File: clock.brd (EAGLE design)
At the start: 100 x 80 mm, 50 parts, among them J3 POWER_JACKSLT, U2 LM75A_SO8, U3 ESP8266_13

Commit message: Worked on the silk
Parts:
- moved TP3 0.76 mm to (18.7, 27.6)
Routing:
- net N$2: track 14.4 -> 13.7 mm
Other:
- board text added: "0318"
- board text added: "1: ADC"
- board text added: "2: LED Data (3V)"
- board text added: "3: LED Data (5V)"
- board text added: "4: LM75A OS"
- board text added: "5: IO2"
- board text added: "6: IO3"
- board text added: "DATA"
- board text added: "IO12"
- board text added: "IO13"
- board text added: "IO14"
- board text added: "IO15"
- board text added: "IO3"
- board text added: "IO4"
- board text added: "IO5"
- board text added: "Testpoints:"
- board text removed: "0218"
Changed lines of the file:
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@@
 <rectangle x1="2.2" y1="44.1" x2="5.8" y2="45.3" layer="51"/>
 <text x="9" y="78" size="1.016" layer="21" font="vector" ratio="12" align="center-left">Rev A</text>
-<text x="9" y="76.5" size="1.016" layer="21" font="vector" ratio="12" align="center-left">0218</text>
+<text x="9" y="76.5" size="1.016" layer="21" font="vector" ratio="12" align="center-left">0318</text>
 <text x="24.7" y="25" size="1.016" layer="21" font="vector" ratio="12" align="center">G</text>
 <dimension x1="3.5" y1="3.5" x2="96.5" y2="3.5" x3="50" y3="-2.6" textsize="1.016" textratio="12" layer="51" dtype="horizontal"/>
@@
 <wire x1="90.99" y1="19.5" x2="90.59" y2="19.9" width="0.127" layer="21"/>
 <wire x1="90.99" y1="18.3" x2="90.59" y2="18.7" width="0.127" layer="21"/>
+<wire x1="22" y1="44" x2="27.6" y2="44" width="0.127" layer="21"/>
+<wire x1="22" y1="36" x2="27.6" y2="36" width="0.127" layer="21"/>
+<wire x1="22" y1="44" x2="22" y2="36" width="0.127" layer="21"/>
+<text x="21" y="40" size="1.016" layer="21" font="vector" ratio="12" rot="R180" align="center-left">DATA</text>
+<wire x1="22" y1="57" x2="27.6" y2="57" width="0.127" layer="21"/>
+<wire x1="22" y1="51" x2="27.6" y2="51" width="0.127" layer="21"/>
+<wire x1="22" y1="57" x2="22" y2="51" width="0.127" layer="21"/>
+<text x="25" y="69.5" size="1.016" layer="22" font="vector" ratio="12" rot="MR0" align="center-left">Testpoints:</text>
+<text x="25" y="66.5" size="1.016" layer="22" font="vector" ratio="12" rot="MR0" align="center-left">1: ADC</text>
+<text x="25" y="64.5" size="1.016" layer="22" font="vector" ratio="12" rot="MR0" align="center-left">2: LED Data (3V)</text>
+<text x="25" y="62.5" size="1.016" layer="22" font="vector" ratio="12" rot="MR0" align="center-left">3: LED Data (5V)</text>
+<text x="25" y="60.5" size="1.016" layer="22" font="vector" ratio="12" rot="MR0" align="center-left">4: LM75A OS</text>
+<text x="25" y="58.5" size="1.016" layer="22" font="vector" ratio="12" rot="MR0" align="center-left">5: IO2</text>
+<text x="25" y="56.5" size="1.016" layer="22" font="vector" ratio="12" rot="MR0" align="center-left">6: IO3</text>
+<wire x1="26" y1="71" x2="26" y2="68" width="0.127" layer="22"/>
+<wire x1="26" y1="68" x2="26" y2="55" width="0.127" layer="22"/>
+<wire x1="26" y1="55" x2="11" y2="55" width="0.127" layer="22"/>
+<wire x1="11" y1="55" x2="11" y2="68" width="0.127" layer="22"/>
+<wire x1="11" y1="68" x2="11" y2="71" width="0.127" layer="22"/>
+<wire x1="26" y1="71" x2="11" y2="71" width="0.127" layer="22"/>
+<wire x1="26" y1="68" x2="11" y2="68" width="0.127" layer="22"/>
+<text x="7.1" y="17.54" size="0.6096" layer="22" font="vector" ratio="12" rot="MR270" align="top-center">IO12</text>
+<text x="7.1" y="15" size="0.6096" layer="22" font="vector" ratio="12" rot="MR270" align="top-center">IO15</text>
+<text x="7.1" y="12.46" size="0.6096" layer="22" font="vector" ratio="12" rot="MR270" align="top-center">IO3</text>
+<text x="7.1" y="9.92" size="0.6096" layer="21" font="vector" ratio="12" rot="R90" align="top-center">SDA</text>
+<text x="7.1" y="9.92" size="0.6096" layer="22" font="vector" ratio="12" rot="MR270" align="top-center">IO4</text>
+<text x="1.1" y="9.92" size="0.6096" layer="22" font="vector" ratio="12" rot="MR270" align="bottom-center">IO5</text>
+<text x="1" y="15" size="0.6096" layer="22" font="vector" ratio="12" rot="MR270" align="bottom-center">IO13</text>
+<text x="1" y="17.54" size="0.6096" layer="22" font="vector" ratio="12" rot="MR270" align="bottom-center">IO14</text>
 </plain>
 <attributes>
@@
 </element>
 <element name="J2" library="Sebastian" package="IEC_C8_RIGHT" value="" x="91" y="60" rot="R270"/>
-<element name="U3" library="Sebastian" package="ESP13" value="ESP8266_13" x="20.5" y="4" rot="R180"/>
+<element name="U3" library="Sebastian" package="ESP13" value="ESP8266_13" x="20.5" y="4" smashed="yes" rot="R180">
+<attribute name="NAME" x="29.5" y="15" size="1.016" layer="25" font="vector" ratio="12" rot="R180" align="center-left"/>
+</element>
 <element name="JP1" library="Sebastian" package="1X3_MOLEX_53254" value="" x="28" y="40" rot="R90"/>
 <element name="J5" library="Sebastian" package="1X2_MOLEX_53254" value="" x="28" y="54" rot="R90"/>
@@
 <attribute name="VALUE" x="18.065" y="24.338" size="0.0254" layer="27"/>
 </element>
-<element name="TP3" library="testpad" package="TP15R" value="TPTP15R" x="18.7" y="28.4" smashed="yes">
-<attribute name="NAME" x="18.7" y="26.8" size="1.016" layer="25" font="vector" ratio="12" align="center"/>
-<attribute name="TP_SIGNAL_NAME" value="" x="18.7" y="25.86" size="1" layer="37"/>
-<attribute name="VALUE" x="18.065" y="27.638" size="0.0254" layer="27"/>
+<element name="TP3" library="testpad" package="TP15R" value="TPTP15R" x="18.7" y="27.64" smashed="yes">
+<attribute name="NAME" x="18.7" y="29.24" size="1.016" layer="25" font="vector" ratio="12" align="center"/>
+<attribute name="TP_SIGNAL_NAME" value="" x="18.7" y="25.1" size="1" layer="37"/>
+<attribute name="VALUE" x="18.065" y="26.878" size="0.0254" layer="27"/>
 </element>
 <element name="TP4" library="testpad" package="TP15R" value="TPTP15R" x="4.5" y="52" smashed="yes">
@@
 <contactref element="TP3" pad="TP"/>
 <wire x1="14.325" y1="21.98740625" x2="16.08740625" y2="21.98740625" width="0.254" layer="1"/>
-<wire x1="16.08740625" y1="21.98740625" x2="17.3" y2="23.2" width="0.254" layer="1"/>
-<wire x1="17.3" y1="23.2" x2="17.3" y2="27" width="0.254" layer="1"/>
-<wire x1="17.3" y1="27" x2="18.7" y2="28.4" width="0.254" layer="1"/>
+<wire x1="17.3" y1="23.2" x2="16.08740625" y2="21.98740625" width="0.254" layer="1"/>
+<wire x1="18.7" y1="27.64" x2="17.3" y2="26.24" width="0.254" layer="1"/>
+<wire x1="17.3" y1="26.24" x2="17.3" y2="23.2" width="0.254" layer="1"/>
 </signal>
 <signal name="L">

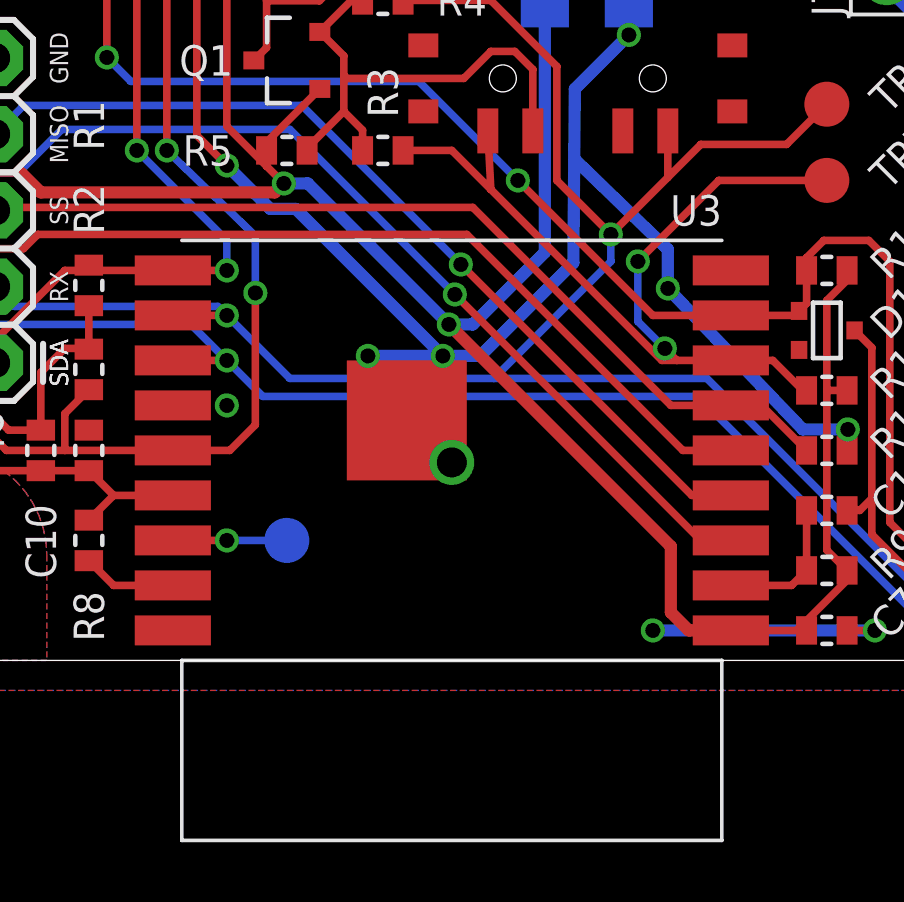
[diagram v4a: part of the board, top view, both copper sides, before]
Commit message: Switched to the new footprint for the ESP8266
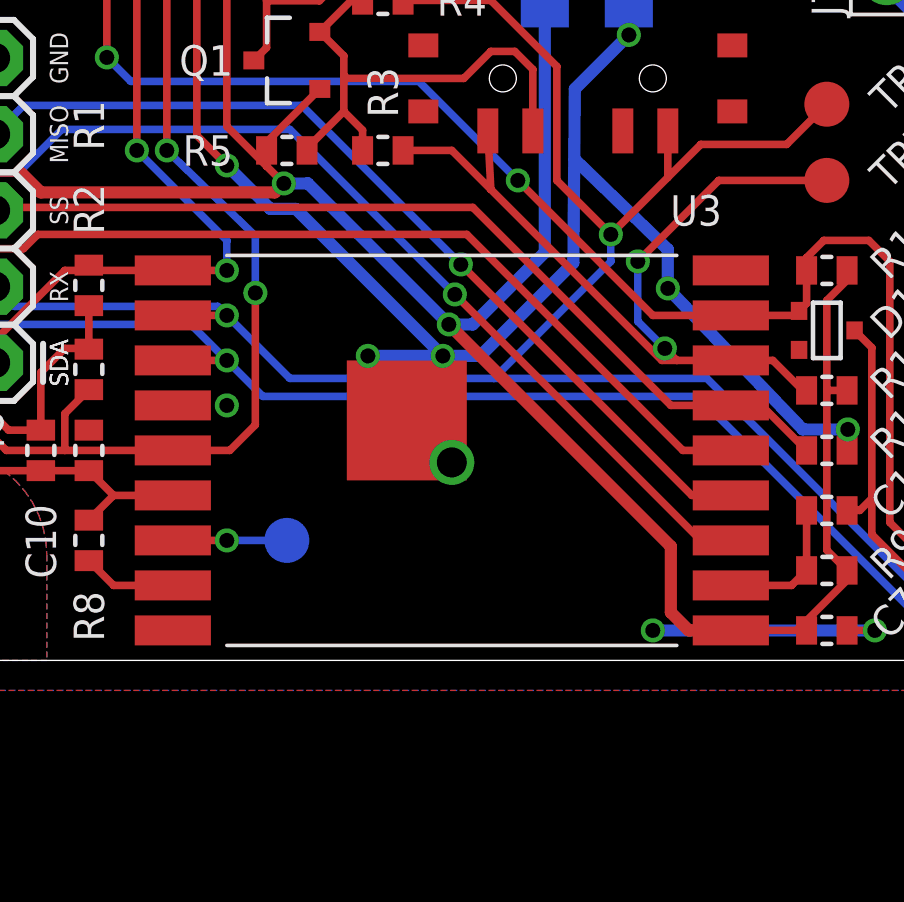
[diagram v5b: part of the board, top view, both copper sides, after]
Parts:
- U3: device Sebastian:ESP13 -> Modules:ESP13
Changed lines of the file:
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@@
 <layers>
 <layer number="1" name="Top" color="4" fill="1" visible="yes" active="yes"/>
+<layer number="2" name="Route2" color="1" fill="3" visible="no" active="no"/>
+<layer number="3" name="Route3" color="4" fill="3" visible="no" active="no"/>
+<layer number="4" name="Route4" color="1" fill="4" visible="no" active="no"/>
+<layer number="5" name="Route5" color="4" fill="4" visible="no" active="no"/>
+<layer number="6" name="Route6" color="1" fill="8" visible="no" active="no"/>
+<layer number="7" name="Route7" color="4" fill="8" visible="no" active="no"/>
+<layer number="8" name="Route8" color="1" fill="2" visible="no" active="no"/>
+<layer number="9" name="Route9" color="4" fill="2" visible="no" active="no"/>
+<layer number="10" name="Route10" color="1" fill="7" visible="no" active="no"/>
+<layer number="11" name="Route11" color="4" fill="7" visible="no" active="no"/>
+<layer number="12" name="Route12" color="1" fill="5" visible="no" active="no"/>
+<layer number="13" name="Route13" color="4" fill="5" visible="no" active="no"/>
+<layer number="14" name="Route14" color="1" fill="6" visible="no" active="no"/>
+<layer number="15" name="Route15" color="4" fill="6" visible="no" active="no"/>
 <layer number="16" name="Bottom" color="1" fill="1" visible="yes" active="yes"/>
 <layer number="17" name="Pads" color="2" fill="1" visible="yes" active="yes"/>
@@
 </element>
 <element name="J2" library="Sebastian" package="IEC_C8_RIGHT" value="" x="91" y="60" rot="R270"/>
-<element name="U3" library="Sebastian" package="ESP13" value="ESP8266_13" x="20.5" y="4" smashed="yes" rot="R180">
-<attribute name="NAME" x="29.5" y="15" size="1.016" layer="25" font="vector" ratio="12" rot="R180" align="center-left"/>
-</element>
+<element name="U3" library="Modules" package="ESP13" value="ESP8266_13" x="20.5" y="4" rot="R180"/>
 <element name="JP1" library="Sebastian" package="1X3_MOLEX_53254" value="" x="28" y="40" rot="R90"/>
 <element name="J5" library="Sebastian" package="1X2_MOLEX_53254" value="" x="28" y="54" rot="R90"/>
@@
 <element name="C2" library="Sebastian" package="0603" value=".1u" x="5" y="70.5" rot="R180"/>
 <element name="C3" library="Sebastian" package="0603" value=".1u" x="5" y="72" rot="R180"/>
-<element name="TP1" library="testpad" package="TP15R" value="TPTP15R" x="15" y="4" smashed="yes" rot="MR0">
+<element name="TP1" library="testpad" library_urn="urn:adsk.eagle:library:385" package="TP15R" package3d_urn="urn:adsk.eagle:package:27968/1" value="TPTP15R" x="15" y="4" smashed="yes" rot="MR0">
 <attribute name="NAME" x="16.4" y="4" size="1.016" layer="26" font="vector" ratio="12" rot="MR180" align="center-left"/>
 <attribute name="TP_SIGNAL_NAME" value="" x="15" y="1.46" size="1" layer="38" rot="MR0"/>
 <attribute name="VALUE" x="15.635" y="3.238" size="0.0254" layer="28" rot="MR0"/>
 </element>
-<element name="TP2" library="testpad" package="TP15R" value="TPTP15R" x="18.7" y="25.1" smashed="yes">
+<element name="TP2" library="testpad" library_urn="urn:adsk.eagle:library:385" package="TP15R" package3d_urn="urn:adsk.eagle:package:27968/1" value="TPTP15R" x="18.7" y="25.1" smashed="yes">
 <attribute name="NAME" x="18.7" y="23.5" size="1.016" layer="25" font="vector" ratio="12" align="center"/>
 <attribute name="TP_SIGNAL_NAME" value="" x="18.7" y="22.56" size="1" layer="37"/>
 <attribute name="VALUE" x="18.065" y="24.338" size="0.0254" layer="27"/>
 </element>
-<element name="TP3" library="testpad" package="TP15R" value="TPTP15R" x="18.7" y="27.64" smashed="yes">
+<element name="TP3" library="testpad" library_urn="urn:adsk.eagle:library:385" package="TP15R" package3d_urn="urn:adsk.eagle:package:27968/1" value="TPTP15R" x="18.7" y="27.64" smashed="yes">
 <attribute name="NAME" x="18.7" y="29.24" size="1.016" layer="25" font="vector" ratio="12" align="center"/>
 <attribute name="TP_SIGNAL_NAME" value="" x="18.7" y="25.1" size="1" layer="37"/>
 <attribute name="VALUE" x="18.065" y="26.878" size="0.0254" layer="27"/>
 </element>
-<element name="TP4" library="testpad" package="TP15R" value="TPTP15R" x="4.5" y="52" smashed="yes">
+<element name="TP4" library="testpad" library_urn="urn:adsk.eagle:library:385" package="TP15R" package3d_urn="urn:adsk.eagle:package:27968/1" value="TPTP15R" x="4.5" y="52" smashed="yes">
 <attribute name="NAME" x="2.7" y="53" size="1.016" layer="25" font="vector" ratio="12" rot="R270" align="center-left"/>
 <attribute name="TP_SIGNAL_NAME" value="" x="4.5" y="49.46" size="1" layer="37"/>
@@
 <attribute name="NAME" x="90" y="19.9" size="1.016" layer="25" font="vector" ratio="12" rot="R180" align="center-left"/>
 </element>
-<element name="TP5" library="testpad" package="TP15R" value="TPTP15R" x="33" y="16" smashed="yes">
+<element name="TP5" library="testpad" library_urn="urn:adsk.eagle:library:385" package="TP15R" package3d_urn="urn:adsk.eagle:package:27968/1" value="TPTP15R" x="33" y="16" smashed="yes">
 <attribute name="NAME" x="34.7" y="16" size="1.016" layer="25" font="vector" ratio="12" rot="R45" align="center-left"/>
 <attribute name="TP_SIGNAL_NAME" value="" x="33" y="13.46" size="1" layer="37"/>
 <attribute name="VALUE" x="32.365" y="15.238" size="0.0254" layer="27"/>
 </element>
-<element name="TP6" library="testpad" package="TP15R" value="TPTP15R" x="33" y="18.54" smashed="yes">
+<element name="TP6" library="testpad" library_urn="urn:adsk.eagle:library:385" package="TP15R" package3d_urn="urn:adsk.eagle:package:27968/1" value="TPTP15R" x="33" y="18.54" smashed="yes">
 <attribute name="NAME" x="34.7" y="18.54" size="1.016" layer="25" font="vector" ratio="12" rot="R45" align="center-left"/>
 <attribute name="TP_SIGNAL_NAME" value="" x="33" y="16" size="1" layer="37"/>
@@
 which will not be processed correctly with this version.
 </note>
+<note version="8.2" severity="warning">
+Since Version 8.2, EAGLE supports online libraries. The ids
+of those online libraries will not be understood (or retained)
+with this version.
+</note>
+<note version="8.3" severity="warning">
+Since Version 8.3, EAGLE supports URNs for individual library
+assets (packages, symbols, and devices). The URNs of those assets
+will not be understood (or retained) with this version.
+</note>
+<note version="8.3" severity="warning">
+Since Version 8.3, EAGLE supports the association of 3D packages
+with devices in libraries, schematics, and board files. Those 3D
+packages will not be understood (or retained) with this version.
+</note>
 </compatibility>
